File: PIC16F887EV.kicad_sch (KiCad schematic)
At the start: 1 part, among them U1 PIC16F887-IP

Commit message: Add files via upload
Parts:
- added R1: R, symbol Device:R
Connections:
- net at U1.37 (AN11/RB4): now also R1.2
- net at U1.5 (C1IN+/Vref+/AN3/RA3): now also R1.1
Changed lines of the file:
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@@
 (kicad_sch (version 20230121) (generator eeschema)
   (paper "A4")
+  (wire (pts (xy 190.5 92.71) (xy 190.5 97.79))
+    (stroke (width 0) (type default))
+  )
+  (wire (pts (xy 190.5 85.09) (xy 190.5 77.47))
+    (stroke (width 0) (type default))
+  )
+  (wire (pts (xy 190.5 97.79) (xy 168.91 97.79))
+    (stroke (width 0) (type default))
+  )
+  (wire (pts (xy 190.5 77.47) (xy 168.91 77.47))
+    (stroke (width 0) (type default))
+  )
   (text "Placa de Evaluación - PIC16F887\nTaller de Electrónica\nFCEFyN - UNC"
     (at 13.97 31.75 0)
@@
         )
       )
+    )
+  )
+  (symbol (lib_id "Device:R") (at 190.5 88.9 0) (unit 1)
+    (in_bom yes) (on_board yes) (dnp no) (fields_autoplaced)
+    (property "Reference" "R1" (at 193.04 87.63 0)
+      (effects (font (size 1.27 1.27)) (justify left))
+    )
+    (property "Value" "R" (at 193.04 90.17 0)
+      (effects (font (size 1.27 1.27)) (justify left))
+    )
+    (property "Footprint" "" (at 188.722 88.9 90)
+      (effects (font (size 1.27 1.27)) hide)
+    )
+    (property "Datasheet" "~" (at 190.5 88.9 0)
+      (effects (font (size 1.27 1.27)) hide)
+    )
+    (pin "1")
+    (pin "2")
+    (instances
+      (project "PIC16F887EV"
+        (path "/a2515825-f12e-4570-8718-6acb93c561c0"
+          (reference "R1") (unit 1)
+        )
+      )

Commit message: Add files via upload
con corto prueba
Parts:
- removed R1: R, symbol Device:R
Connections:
- net at U1.1 (RE3/~{MCLR}/Vpp): now also U1.10 (RE2/AN7)
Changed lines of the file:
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@@
 (kicad_sch (version 20230121) (generator eeschema)
   (paper "A4")
-  (wire (pts (xy 190.5 92.71) (xy 190.5 97.79))
+  (wire (pts (xy 78.74 69.85) (xy 78.74 115.57))
     (stroke (width 0) (type default))
   )
-  (wire (pts (xy 190.5 85.09) (xy 190.5 77.47))
+  (wire (pts (xy 113.03 69.85) (xy 78.74 69.85))
     (stroke (width 0) (type default))
   )
-  (wire (pts (xy 190.5 97.79) (xy 168.91 97.79))
-    (stroke (width 0) (type default))
-  )
-  (wire (pts (xy 190.5 77.47) (xy 168.91 77.47))
+  (wire (pts (xy 78.74 115.57) (xy 113.03 115.57))
     (stroke (width 0) (type default))
   )
@@
         )
       )
-    )
-  )
-  (symbol (lib_id "Device:R") (at 190.5 88.9 0) (unit 1)
-    (in_bom yes) (on_board yes) (dnp no) (fields_autoplaced)
-    (property "Reference" "R1" (at 193.04 87.63 0)
-      (effects (font (size 1.27 1.27)) (justify left))
-    )
-    (property "Value" "R" (at 193.04 90.17 0)
-      (effects (font (size 1.27 1.27)) (justify left))
-    )
-    (property "Footprint" "" (at 188.722 88.9 90)
-      (effects (font (size 1.27 1.27)) hide)
-    )
-    (property "Datasheet" "~" (at 190.5 88.9 0)
-      (effects (font (size 1.27 1.27)) hide)
-    )
-    (pin "1")
-    (pin "2")
-    (instances
-      (project "PIC16F887EV"
-        (path "/a2515825-f12e-4570-8718-6acb93c561c0"
-          (reference "R1") (unit 1)
-        )
-      )

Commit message: Update PIC16F887EV.kicad_sch
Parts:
- added BZ1: Buzzer, Buzzer_Beeper:Buzzer_12x9.5RM7.6, symbol Device:Buzzer
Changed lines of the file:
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@@
+    )
+  )
+  (symbol (lib_id "Device:Buzzer") (at 204.47 69.85 0) (unit 1)
+    (in_bom yes) (on_board yes) (dnp no) (fields_autoplaced)
+    (property "Reference" "BZ1" (at 208.28 68.58 0)
+      (effects (font (size 1.27 1.27)) (justify left))
+    )
+    (property "Value" "Buzzer" (at 208.28 71.12 0)
+      (effects (font (size 1.27 1.27)) (justify left))
+    )
+    (property "Footprint" "Buzzer_Beeper:Buzzer_12x9.5RM7.6" (at 203.835 67.31 90)
+      (effects (font (size 1.27 1.27)) hide)
+    )
+    (property "Datasheet" "~" (at 203.835 67.31 90)
+      (effects (font (size 1.27 1.27)) hide)
+    )
+    (pin "1")
+    (pin "2")
+    (instances
+      (project "PIC16F887EV"
+        (path "/a2515825-f12e-4570-8718-6acb93c561c0"
+          (reference "BZ1") (unit 1)
+        )
+      )
     )
   )

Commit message: Buzzer Agregado
Hay que elegir el footprint correcto
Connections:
- net at U1.33 (INT/AN12/RB0): now also BZ1.1 (-)
- net GND: now reaches BZ1.2 (+)
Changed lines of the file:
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@@
+    (stroke (width 0) (type default))
+  )
+  (wire (pts (xy 201.93 67.31) (xy 180.34 67.31))
+    (stroke (width 0) (type default))
+  )
+  (wire (pts (xy 180.34 67.31) (xy 180.34 87.63))
     (stroke (width 0) (type default))
   )
   (wire (pts (xy 113.03 69.85) (xy 78.74 69.85))
+    (stroke (width 0) (type default))
+  )
+  (wire (pts (xy 168.91 87.63) (xy 180.34 87.63))
     (stroke (width 0) (type default))
   )
@@
         )
       )
+    )
+  )
+  (symbol (lib_id "power:GND") (at 201.93 72.39 0) (unit 1)
+    (in_bom yes) (on_board yes) (dnp no) (fields_autoplaced)
+    (property "Reference" "#PWR01" (at 201.93 78.74 0)
+      (effects (font (size 1.27 1.27)) hide)
+    )
+    (property "Value" "GND" (at 201.93 77.47 0)
+      (effects (font (size 1.27 1.27)))
+    )
+    (property "Footprint" "" (at 201.93 72.39 0)
+      (effects (font (size 1.27 1.27)) hide)
+    )
+    (property "Datasheet" "" (at 201.93 72.39 0)
+      (effects (font (size 1.27 1.27)) hide)
+    )
+    (pin "1")
+    (instances
+      (project "PIC16F887EV"
+        (path "/a2515825-f12e-4570-8718-6acb93c561c0"
+          (reference "#PWR01") (unit 1)
+        )
+      )

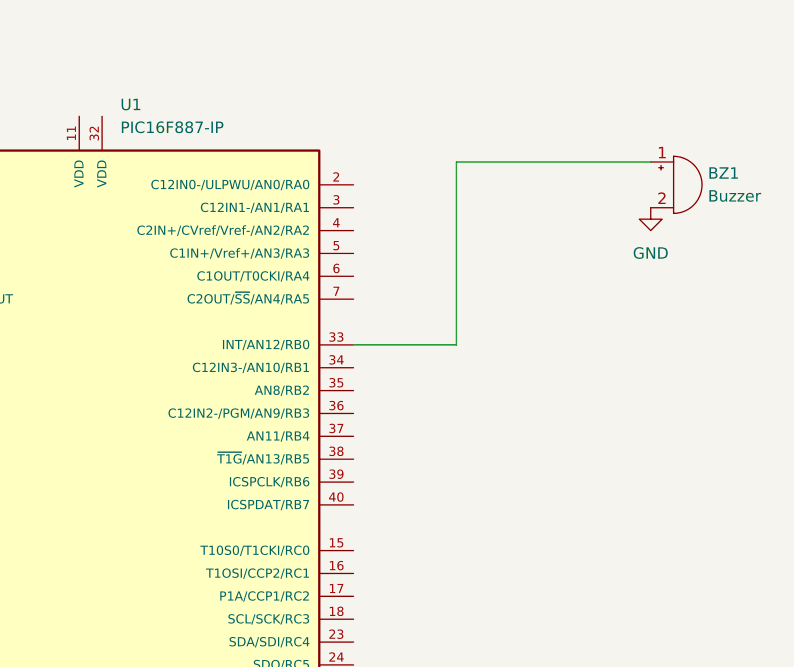
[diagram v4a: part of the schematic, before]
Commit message: cambio de pin a n 7
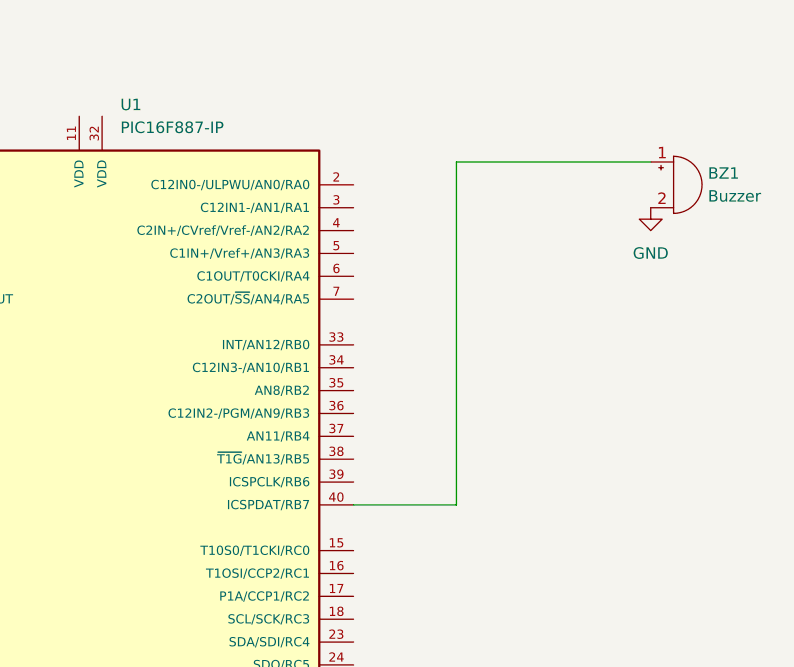
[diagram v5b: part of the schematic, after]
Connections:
- net at U1.33 (INT/AN12/RB0): no longer BZ1.1 (-)
- net at U1.40 (ICSPDAT/RB7): now also BZ1.1 (-)
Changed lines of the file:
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@@
 (kicad_sch (version 20230121) (generator eeschema)
   (paper "A4")
+  (wire (pts (xy 168.91 105.41) (xy 180.34 105.41))
+    (stroke (width 0) (type default))
+  )
   (wire (pts (xy 78.74 69.85) (xy 78.74 115.57))
     (stroke (width 0) (type default))
@@
     (stroke (width 0) (type default))
   )
-  (wire (pts (xy 180.34 67.31) (xy 180.34 87.63))
+  (wire (pts (xy 180.34 67.31) (xy 180.34 105.41))
     (stroke (width 0) (type default))
   )
@@
     (stroke (width 0) (type default))
   )
-  (wire (pts (xy 168.91 87.63) (xy 180.34 87.63))
-    (stroke (width 0) (type default))
-  )

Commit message: DoblePin
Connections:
- net at U1.15 (T10S0/T1CKI/RC0): now also BZ1.1 (-), U1.40 (ICSPDAT/RB7)
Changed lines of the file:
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@@
 (kicad_sch (version 20230121) (generator eeschema)
   (paper "A4")
+  (junction (at 180.34 105.41) (diameter 0) (color 0 0 0 0)
+  )
+  (wire (pts (xy 180.34 105.41) (xy 180.34 110.49))
+    (stroke (width 0) (type default))
+  )
   (wire (pts (xy 168.91 105.41) (xy 180.34 105.41))
     (stroke (width 0) (type default))
@@
     (stroke (width 0) (type default))
   )
+  (wire (pts (xy 168.91 110.49) (xy 180.34 110.49))
+    (stroke (width 0) (type default))
+  )
